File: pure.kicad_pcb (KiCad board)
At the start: 2 copper layers, 100 x 90 mm, 146 parts, among them CON1 AVR-ISP-6, J1 JACK_TRS_3pins, J10 Conn_01x01, J11 Conn_01x01, J12 Conn_01x01, J13 Conn_Coaxial, J5 JACK_TRS_3pins, J7 ANT, J8 Jack-DC, J9 Conn_01x01, K1 TQ2-12VDC, K2 RS-12, Q1 2N7002, Q2 2N7002, Q3 MMBT2222, Q4 BD139, U1 MS5351, U15 74LVC74, U16 NE5532, U2 ATMEGA328P-AU, U3 MC33079, U4 4051, Y1 25..27Mhz

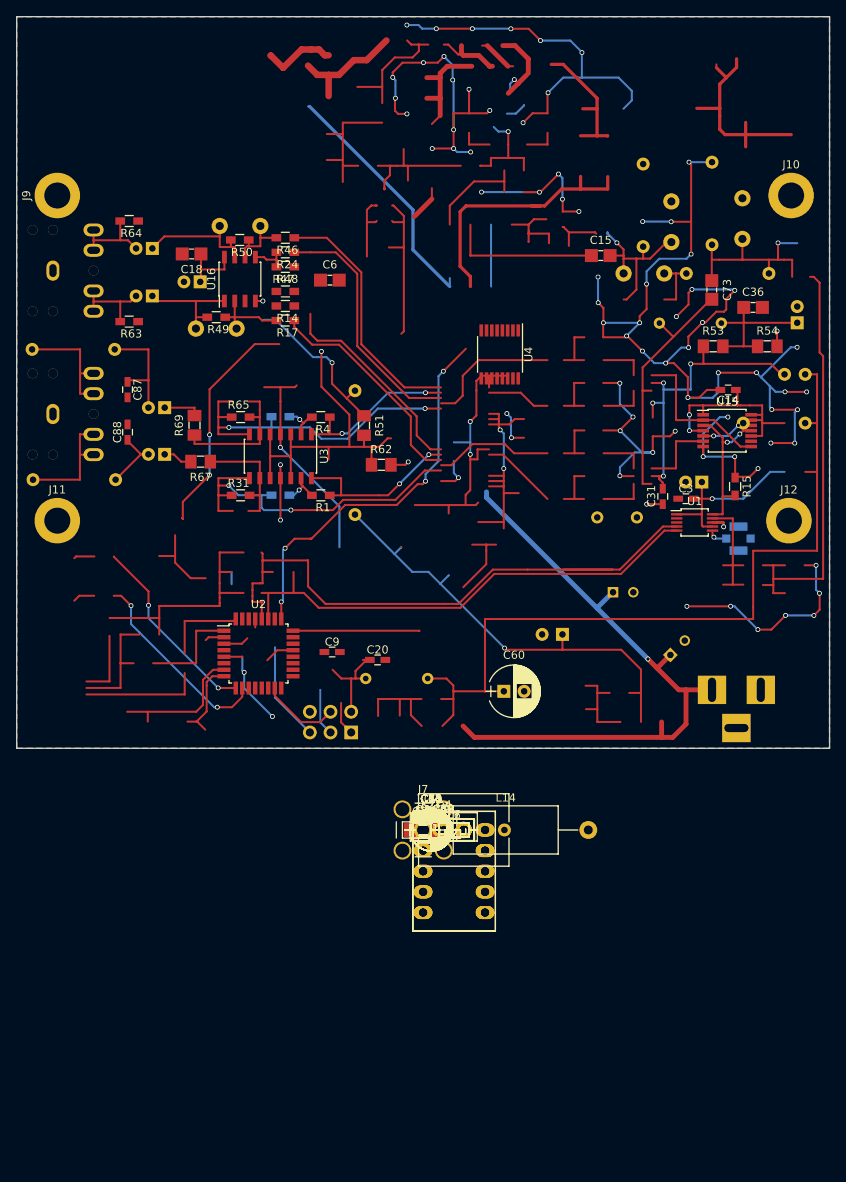
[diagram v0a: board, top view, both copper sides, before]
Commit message: schematics mixer progress, 74HC4053, IF RX. PCB update
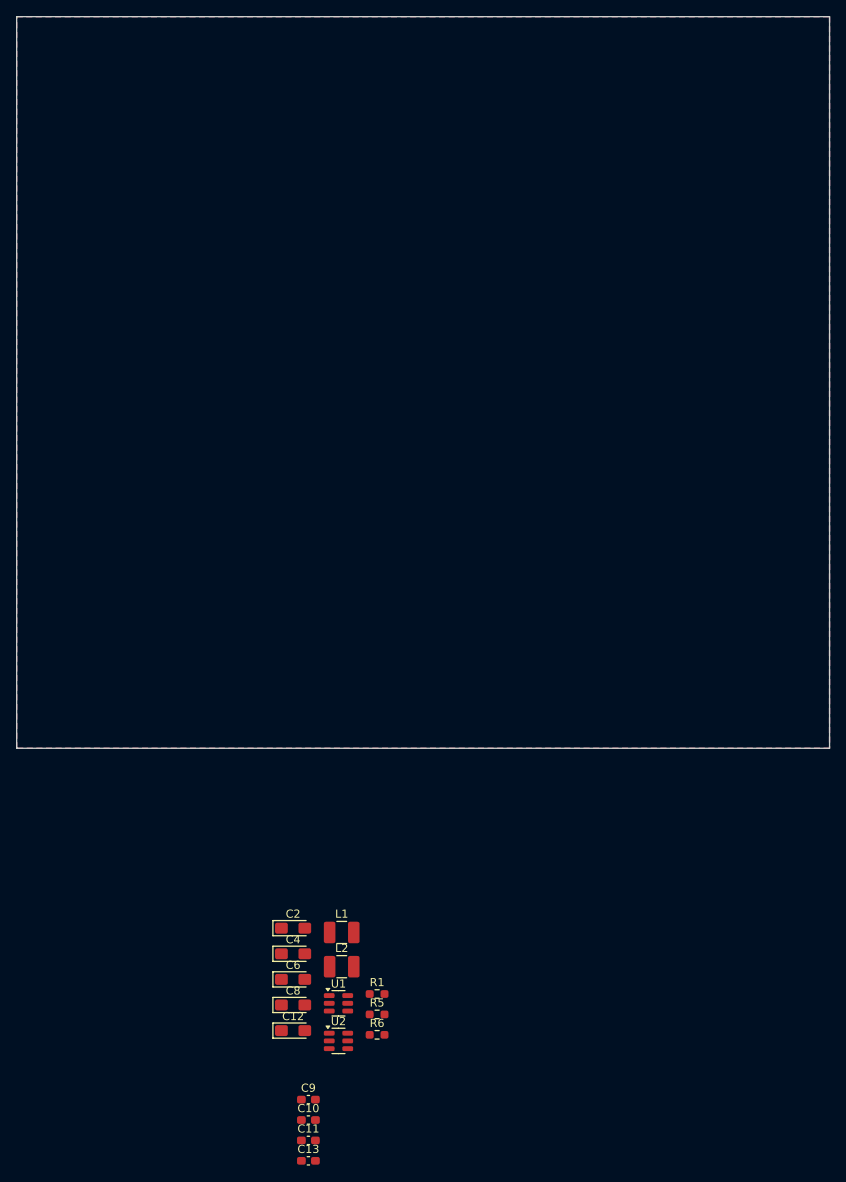
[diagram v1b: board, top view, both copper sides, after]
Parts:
- removed C1, C22: 820(390)pF, LCSDR:C_Disc_D7.5mm_W2.5mm_P5.00mm
- removed C14, C20, C23, C26, C3, C64: 100nF, Capacitors_SMD:C_0603_HandSoldering
- removed C15, C18, C36, C41, C43, C73: 100nF, LCSDR:C_1206_0603
- removed C16, C17: 220pF, LCSDR:C_Disc_D7.5mm_W2.5mm_P5.00mm
- removed C19, C21, C33, C34, C40, C45, C7: 10uF, LCSDR:CP_Radial_D5.0mm_P2.00mm
- removed C24, C57: 220uF, LCSDR:C_Radial_D5_L11_P2.5
- removed C25, C5: 27nF, LCSDR:C_1206_0603
- removed C27: 390(200)pF, LCSDR:C_Disc_D7.5mm_W2.5mm_P5.00mm
- removed C28, C32, C35, C62, C63: 10uF, Capacitors_THT:CP_Radial_D5.0mm_P2.00mm
- removed C29, C30, C87, C88: 27nF, Capacitors_SMD:C_0603_HandSoldering
- removed C31: 100nF, LCSDR:C_0603_HandSoldering
- removed C37: 15nF, LCSDR:C_0603_HandSoldering
- removed C38: 47nF, LCSDR:C_1206_0603
- removed C39: 100nF, LCSDR:C_1206
- removed C48, C49: 100nF, LCSDR:C_Disc_D7.5mm_W2.5mm_P5.00mm
- removed C52, C55: 1nF, LCSDR:C_Disc_D7.5mm_W2.5mm_P5.00mm
- removed C60, C61: 100uF, Capacitors_THT:CP_Radial_D6.3mm_P2.50mm
- removed C71, C72: 2.2uF, LCSDR:CP_Radial_D5.0mm_P2.00mm
- removed CON1: AVR-ISP-6, Pin_Headers:Pin_Header_Straight_2x03_Pitch2.54mm
- removed D1: LL4148, Diodes_SMD:D_MiniMELF
- removed E1: SPARK_GAP, LCSDR:C_Rect_L11.0mm_W8.8mm_P10.00mm_MKT
- removed J1, J5: JACK_TRS_3pins, LCSDR:audio_jack_3_5mm_PJ307
- removed J10, J11, J12, J9: Conn_01x01, Mounting_Holes:MountingHole_3.2mm_M3_DIN965_Pad
- removed J13: Conn_Coaxial, LCSDR:U.FL_Molex_MCRF_73412-0110_Vertical
- removed J7: ANT, Connectors:SMA_THT_Jack_Straight
- removed J8: Jack-DC, LCSDR:BARREL_JACK
- removed K1: TQ2-12VDC, Relays_THT:Relay_DPDT_FRT5
- removed K2: RS-12, Relays_THT:Relay_DPDT_FRT5
- removed L10: 100uH, Inductors_THT:L_Axial_L5.3mm_D2.2mm_P7.62mm_Horizontal_Vishay_IM-1
- removed L11, L15, L6, L7: 100uH, Resistors_THT:R_Axial_DIN0204_L3.6mm_D1.6mm_P7.62mm_Horizontal
- removed L14: 1uH, Inductors_THT:L_Axial_L12.8mm_D5.8mm_P20.32mm_Horizontal_Fastron_HBCC
- removed L16: 47uH, LCSDR:R_Axial_DIN0309_L9.0mm_D3.2mm_P2.54mm_Vertical
- removed L3: 100uH, Resistors_THT:R_Axial_DIN0207_L6.3mm_D2.5mm_P15.24mm_Horizontal
- removed L4: 1(0.47)uH, LCSDR:R_Axial_DIN0207_L6.3mm_D2.5mm_P10.16mm_Horizontal
- removed L5: 2.2(1)uH, LCSDR:R_Axial_DIN0207_L6.3mm_D2.5mm_P10.16mm_Horizontal
- removed L8, L9: 4.7mH, LCSDR:R_Axial_DIN0207_L6.3mm_D2.5mm_P10.16mm_Horizontal
- removed Q1, Q2: 2N7002, TO_SOT_Packages_SMD:SOT-23
- removed Q3: MMBT2222, LCSDR:SOT-23
- removed Q4: BD139, TO_SOT_Packages_THT:TO-126_Vertical
- removed R10: 10, LCSDR:R_1206_0603
- removed R11: 2.2k, LCSDR:R_1206_0603
- removed R12, R19: 33, LCSDR:R_0603_HandSoldering
- removed R13, R28: 330, Resistors_SMD:R_0603_HandSoldering
- removed R14, R17, R21, R24, R46: 1k, LCSDR:R_0603_HandSoldering
- removed R15: 200R*, Resistors_SMD:R_0603_HandSoldering
- removed R16: 470, LCSDR:R_1206_0603
- removed R18, R27: 330, LCSDR:R_0603_HandSoldering
- removed R2, R3, R32, R33: 33R, LCSDR:R_1206_0603
- removed R20: 56, LCSDR:R_0603_HandSoldering
- removed R22, R23: 10k, LCSDR:R_1206_0603
- removed R25, R35, R36, R9: 33, Resistors_SMD:R_0603_HandSoldering
- removed R26, R29, R31, R4, R63, R64, R65: 10k, LCSDR:R_0603_HandSoldering
- removed R39: 5.1, LCSDR:R_0603_HandSoldering
- removed R47, R48, R49, R50: 22k, LCSDR:R_0603_HandSoldering
- removed R51, R62, R67, R69: 1k, LCSDR:R_1206_0603
- removed R53, R54: 510R, LCSDR:R_1206_0603
- removed R56: 68, Resistors_SMD:R_0603_HandSoldering
- removed R7, R8: 6.8k, Resistors_SMD:R_0603_HandSoldering
- removed U15: 74LVC74, Housings_SSOP:TSSOP-14_4.4x5mm_Pitch0.65mm
- removed U16: NE5532, Housings_SOIC:SOIC-8_3.9x4.9mm_Pitch1.27mm
- removed U3: MC33079, Housings_SOIC:SOIC-14_3.9x8.7mm_Pitch1.27mm
- removed U4: 4051, Housings_SSOP:TSSOP-16_4.4x5mm_Pitch0.65mm
- removed Y1: 25..27Mhz, Crystals:Crystal_HC49-U_Vertical
- added L2: 100uH, Inductor_SMD:L_1210_3225Metric_Pad1.42x2.65mm_HandSolder, F.Cu at (105.0, 156.9)
- C10, C13: value 10uF -> 100nF; footprint LCSDR:CP_Radial_D5.0mm_P2.00mm -> Capacitor_SMD:C_0603_1608Metric_Pad1.08x0.95mm_HandSolder
- C11: value 27nF -> 100nF; footprint Capacitors_SMD:C_0603_HandSoldering -> Capacitor_SMD:C_0603_1608Metric_Pad1.08x0.95mm_HandSolder
- C12: value 27nF -> 10uF; footprint Capacitors_SMD:C_0603_HandSoldering -> Capacitor_Tantalum_SMD:CP_EIA-3216-18_Kemet-A_Pad1.58x1.35mm_HandSolder
- C2: footprint LCSDR:CP_Radial_D5.0mm_P2.00mm -> Capacitor_Tantalum_SMD:CP_EIA-3216-18_Kemet-A_Pad1.58x1.35mm_HandSolder; moved to F.Cu
- C4, C8: value 27nF -> 10uF; footprint LCSDR:C_1206_0603 -> Capacitor_Tantalum_SMD:CP_EIA-3216-18_Kemet-A_Pad1.58x1.35mm_HandSolder
- C6: value 100nF -> 10uF; footprint LCSDR:C_1206_0603 -> Capacitor_Tantalum_SMD:CP_EIA-3216-18_Kemet-A_Pad1.58x1.35mm_HandSolder
- C9: value 100nF -> 1uF; footprint Capacitors_SMD:C_0603_HandSoldering -> Capacitor_SMD:C_0603_1608Metric_Pad1.08x0.95mm_HandSolder
- L1: value 1(0.47)uH -> 100uH; footprint LCSDR:R_Axial_DIN0207_L6.3mm_D2.5mm_P10.16mm_Horizontal -> Inductor_SMD:L_1210_3225Metric_Pad1.42x2.65mm_HandSolder; moved to F.Cu
- R1: value 10k -> 20R; footprint LCSDR:R_0603_HandSoldering -> Resistor_SMD:R_0603_1608Metric_Pad0.98x0.95mm_HandSolder
- R5, R6: value 6.8k -> 1k; footprint Resistors_SMD:R_0603_HandSoldering -> Resistor_SMD:R_0603_1608Metric_Pad0.98x0.95mm_HandSolder
- U1: value MS5351 -> SN74LVC1G3157DBVR; footprint LCSDR:MSOP-10_3x3mm_Pitch0.5mm -> Package_TO_SOT_SMD:SOT-23-6
- U2: value ATMEGA328P-AU -> SN74LVC1G3157DBVR; footprint Housings_QFP:TQFP-32_7x7mm_Pitch0.8mm -> Package_TO_SOT_SMD:SOT-23-6
- moved L1 96.1 mm to (105.0, 152.7), turned to 0 degrees
- moved C6 86.1 mm to (99.0, 158.4)
- moved C2 74.4 mm to (99.0, 152.1), turned to 0 degrees
- moved U1 73.6 mm to (104.6, 161.4)
- moved R1 61.7 mm to (109.3, 160.2), turned to 0 degrees
- moved C9 55.1 mm to (100.9, 173.2)
- moved U2 48.7 mm to (104.6, 166.0)
- moved C13 43.1 mm to (100.9, 180.8)
- moved C11 40.7 mm to (100.9, 178.2)
- moved C10 38.4 mm to (100.9, 175.7)
- moved C12 29.4 mm to (99.0, 164.7)
- moved C8 26.8 mm to (99.0, 161.6)
- moved R6 25.8 mm to (109.3, 165.2)
- moved R5 23.4 mm to (109.3, 162.7)
- moved C4 22.1 mm to (99.0, 155.3)
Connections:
- C10 pad 1: IF_TX_U -> GND
- C10 pad 2: GND -> Net-(U1B-V+)
- C11 pad 1: Net-(C11-Pad1) -> GND
- C11 pad 2: GND -> Net-(C11-Pad2)
- C12 pad 1: Net-(C12-Pad1) -> Net-(C11-Pad2)
- C13 pad 1: Net-(C13-Pad1) -> BPF
- C13 pad 2: Net-(C11-Pad1) -> Net-(C13-Pad2)
- C2 pad 1: Net-(C2-Pad1) -> P180
- C2 pad 2: GND -> Net-(C1-Pad1)
- C4 pad 1: Net-(C32-Pad2) -> P0
- C4 pad 2: GND -> Net-(C3-Pad1)
- C6 pad 1: U_0.5 -> P270
- C6 pad 2: GND -> Net-(C5-Pad1)
- C8 pad 1: Net-(C62-Pad2) -> P90
- C8 pad 2: GND -> Net-(C7-Pad1)
- C9 pad 1: Net-(C9-Pad1) -> GND
- C9 pad 2: GND -> Net-(U1B-V+)
- L1 pad 1: Net-(C1-Pad1) -> +3.3V
- L1 pad 2: GND -> Net-(U1B-V+)
- R1 pad 2: Net-(R1-Pad2) -> Net-(C1-Pad1)
- R5 pad 1: +5V -> +3.3V
- R5 pad 2: SCL -> Net-(C11-Pad2)
- R6 pad 1: +5V -> Net-(C11-Pad2)
- R6 pad 2: SDA -> GND
- U1 pad 1: Net-(C2-Pad1) -> Net-(R2-Pad1)
- U1 pad 2: Net-(U1-Pad2) -> GND
- U1 pad 3: Net-(U1-Pad3) -> Net-(R1-Pad1)
- U1 pad 4: Net-(Q1-Pad2) -> Net-(C13-Pad2)
- U1 pad 5: Net-(Q2-Pad2) -> Net-(U1B-V+)
- U1 pad 6: Net-(J13-Pad1) -> J0
- U2 pad 1: (no net) -> Net-(R4-Pad1)
- U2 pad 2: (no net) -> GND
- U2 pad 3: GND -> Net-(R3-Pad1)
- U2 pad 4: Net-(C20-Pad1) -> Net-(C13-Pad2)
- U2 pad 5: GND -> Net-(U1B-V+)
- U2 pad 6: Net-(C20-Pad1) -> J90
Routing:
- net (no net): track 1038.4 -> 0.00 mm, vias 59 -> 0
- net GND: track 196.0 -> 0.00 mm, vias 41 -> 0
- net +12V: track 122.3 -> 0.00 mm, vias 2 -> 0
- net +3V3: track 97.2 -> 0.00 mm
- net Net-(R26-Pad2): track 40.5 -> 0.00 mm, vias 1 -> 0
- net Net-(Q1-Pad2): track 38.7 -> 0.00 mm
- net SCL: track 38.2 -> 0.00 mm
- net Net-(R28-Pad2): track 37.1 -> 0.00 mm, vias 1 -> 0
- net U_0.5: track 34.8 -> 0.00 mm, vias 1 -> 0
- net VCC: track 32.6 -> 0.00 mm, vias 4 -> 0
- net SDA: track 31.0 -> 0.00 mm
- net Net-(C73-Pad2): track 30.9 -> 0.00 mm
- net Net-(C63-Pad1): track 30.9 -> 0.00 mm
- net Net-(C62-Pad1): track 30.7 -> 0.00 mm
- net Net-(Q2-Pad2): track 30.5 -> 0.00 mm
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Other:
- net class Default removed

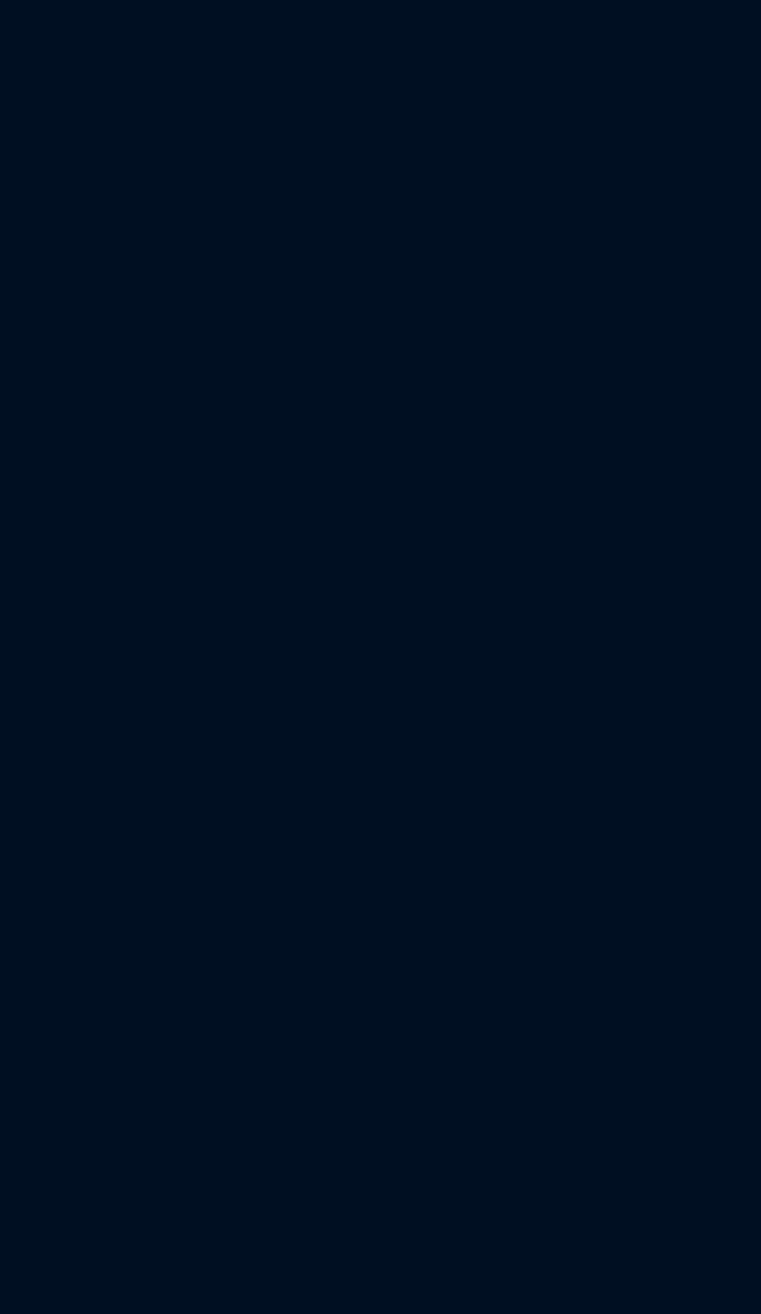
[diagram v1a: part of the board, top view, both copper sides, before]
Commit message: schematics mixer, 74HC4053. IF RX needs JLCPCB numbers. PCB update
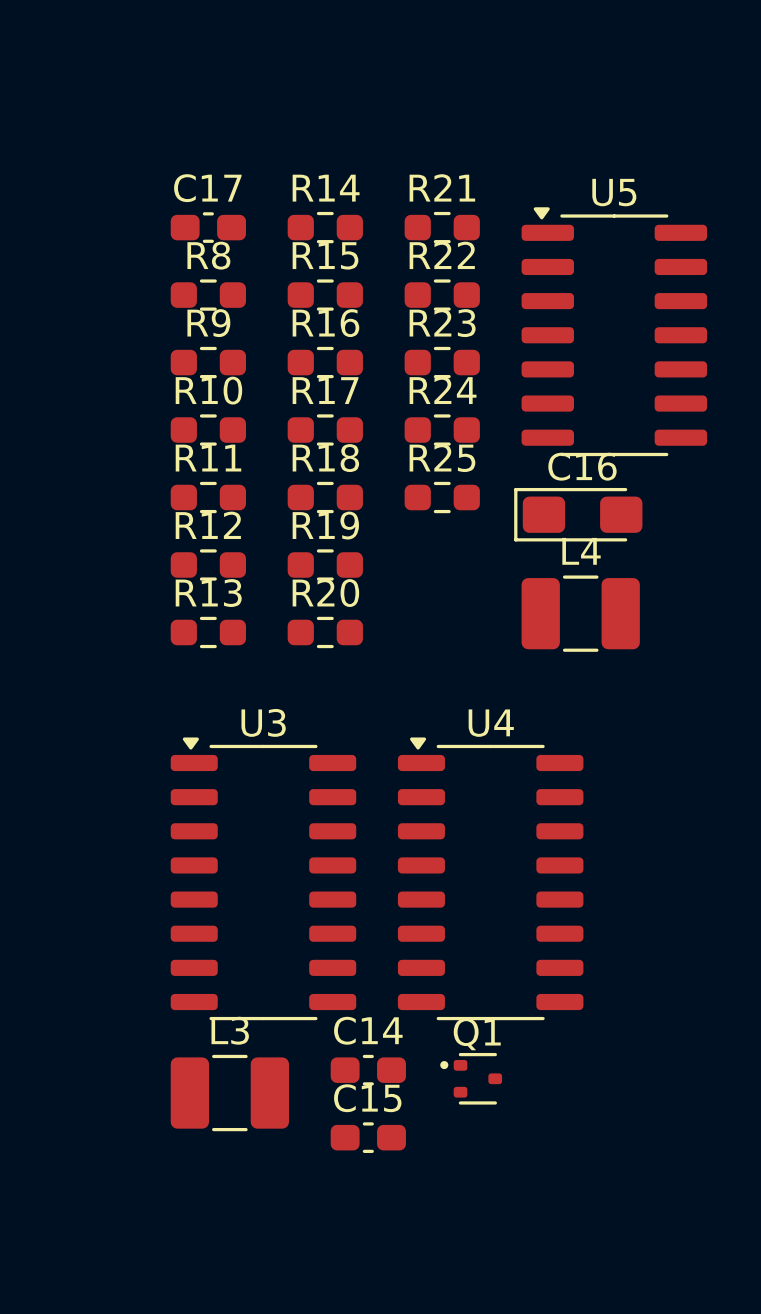
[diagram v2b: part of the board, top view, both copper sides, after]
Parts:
- added C14: 100nF, Capacitor_SMD:C_0603_1608Metric_Pad1.08x0.95mm_HandSolder, F.Cu at (217.9, 141.7)
- added C15: 100nF, Capacitor_SMD:C_0603_1608Metric_Pad1.08x0.95mm_HandSolder, F.Cu at (217.9, 144.2)
- added C16: 10uF, Capacitor_Tantalum_SMD:CP_EIA-3216-18_Kemet-A_Pad1.58x1.35mm_HandSolder, F.Cu at (225.8, 121.0)
- added C17: 100nF, Capacitor_SMD:C_0603_1608Metric_Pad1.08x0.95mm_HandSolder, F.Cu at (211.9, 110.3)
- added L3: 100uH, Inductor_SMD:L_1210_3225Metric_Pad1.42x2.65mm_HandSolder, F.Cu at (212.7, 142.5)
- added L4: 100uH, Inductor_SMD:L_1210_3225Metric_Pad1.42x2.65mm_HandSolder, F.Cu at (225.8, 124.7)
- added Q1: DTC143Z, Package_TO_SOT_SMD:SOT-523, F.Cu at (221.9, 142.0)
- added R10: 300, Resistor_SMD:R_0603_1608Metric_Pad0.98x0.95mm_HandSolder, F.Cu at (211.9, 117.8)
- added R11: 100, Resistor_SMD:R_0603_1608Metric_Pad0.98x0.95mm_HandSolder, F.Cu at (211.9, 120.4)
- added R12: 1k, Resistor_SMD:R_0603_1608Metric_Pad0.98x0.95mm_HandSolder, F.Cu at (211.9, 122.9)
- added R13: 3k, Resistor_SMD:R_0603_1608Metric_Pad0.98x0.95mm_HandSolder, F.Cu at (211.9, 125.4)
- added R14: 3k, Resistor_SMD:R_0603_1608Metric_Pad0.98x0.95mm_HandSolder, F.Cu at (216.3, 110.3)
- added R15: 3k, Resistor_SMD:R_0603_1608Metric_Pad0.98x0.95mm_HandSolder, F.Cu at (216.3, 112.8)
- added R16: 300, Resistor_SMD:R_0603_1608Metric_Pad0.98x0.95mm_HandSolder, F.Cu at (216.3, 115.3)
- added R17: 100, Resistor_SMD:R_0603_1608Metric_Pad0.98x0.95mm_HandSolder, F.Cu at (216.3, 117.8)
- added R18: 3k, Resistor_SMD:R_0603_1608Metric_Pad0.98x0.95mm_HandSolder, F.Cu at (216.3, 120.4)
- added R19: 1k, Resistor_SMD:R_0603_1608Metric_Pad0.98x0.95mm_HandSolder, F.Cu at (216.3, 122.9)
- added R20: 1k, Resistor_SMD:R_0603_1608Metric_Pad0.98x0.95mm_HandSolder, F.Cu at (216.3, 125.4)
- added R21: 3k, Resistor_SMD:R_0603_1608Metric_Pad0.98x0.95mm_HandSolder, F.Cu at (220.6, 110.3)
- added R22: 3k, Resistor_SMD:R_0603_1608Metric_Pad0.98x0.95mm_HandSolder, F.Cu at (220.6, 112.8)
- added R23: 3k, Resistor_SMD:R_0603_1608Metric_Pad0.98x0.95mm_HandSolder, F.Cu at (220.6, 115.3)
- added R24: 750, Resistor_SMD:R_0603_1608Metric_Pad0.98x0.95mm_HandSolder, F.Cu at (220.6, 117.8)
- added R25: 750, Resistor_SMD:R_0603_1608Metric_Pad0.98x0.95mm_HandSolder, F.Cu at (220.6, 120.4)
- added R8: 3k, Resistor_SMD:R_0603_1608Metric_Pad0.98x0.95mm_HandSolder, F.Cu at (211.9, 112.8)
- added R9: 1k, Resistor_SMD:R_0603_1608Metric_Pad0.98x0.95mm_HandSolder, F.Cu at (211.9, 115.3)
- added U3: 74HC4053, Package_SO:SO-16_3.9x9.9mm_P1.27mm, F.Cu at (214.0, 134.7)
- added U4: 74HC4053, Package_SO:SO-16_3.9x9.9mm_P1.27mm, F.Cu at (222.4, 134.7)
- added U5: MC33079, Package_SO:SOIC-14_3.9x8.7mm_P1.27mm, F.Cu at (227.0, 114.3)

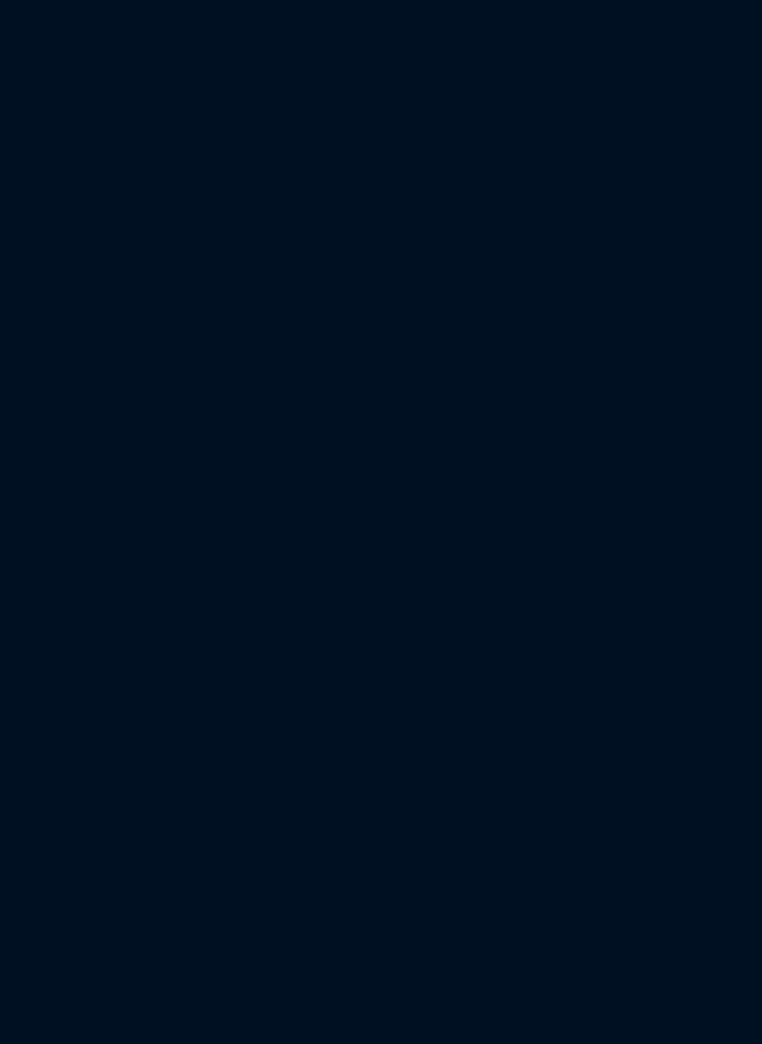
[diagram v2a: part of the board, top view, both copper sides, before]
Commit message: some minor changes, IF RX, 74HC4053, page numbers
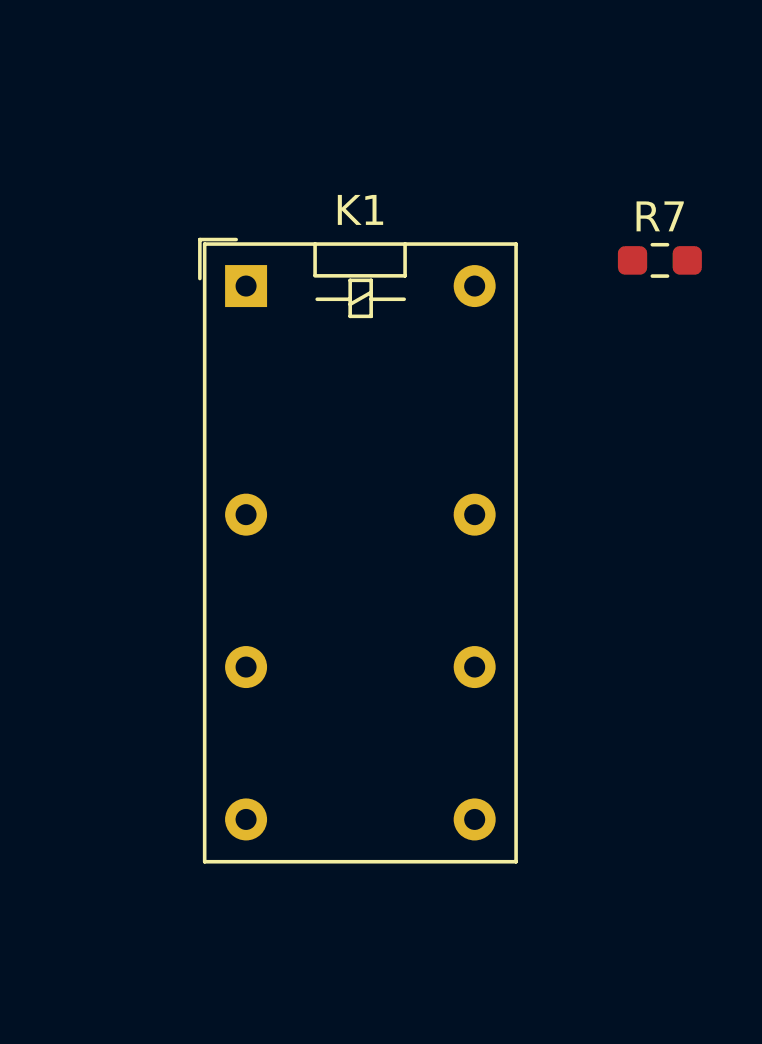
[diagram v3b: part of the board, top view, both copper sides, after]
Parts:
- added K1: G5V-2_Split, Relay_THT:Relay_DPDT_Omron_G5V-2, F.Cu at (218.9, 68.7)
- added R7: 10k, Resistor_SMD:R_0603_1608Metric_Pad0.98x0.95mm_HandSolder, F.Cu at (232.7, 67.9)
